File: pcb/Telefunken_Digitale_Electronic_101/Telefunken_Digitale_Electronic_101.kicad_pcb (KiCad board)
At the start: 2 copper layers, 100 x 52 mm, 31 parts, among them J1 Conn_01x02_MountingPin, J2 Conn_01x02_MountingPin, J3 Conn_01x04_MountingPin, J4 Conn_01x02_Socket, J5 Conn_01x02_Socket, J6 Conn_01x02_Socket, J7 Conn_01x02_Socket, J8 Conn_01x02_Socket, SW1 SW_Push, SW2 SW_Push, U1 DS3231, U2 TM1637_SOP20

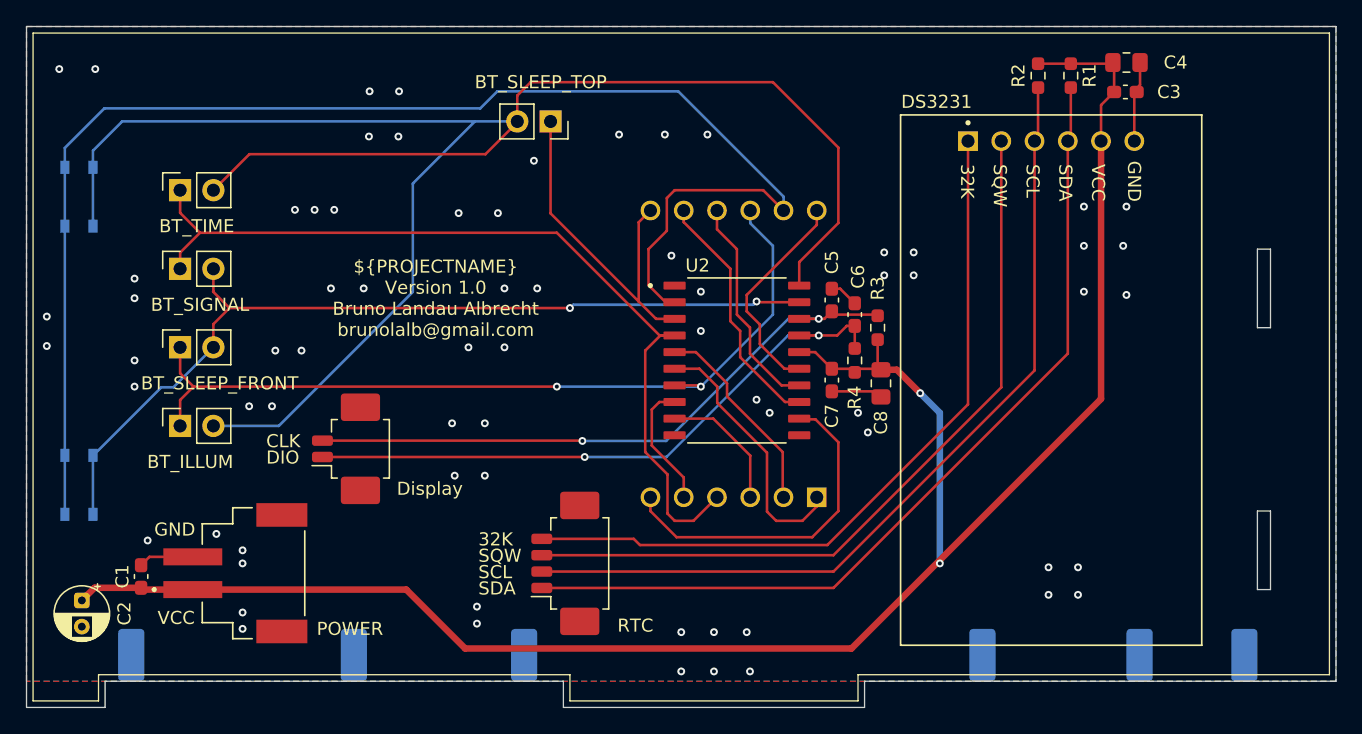
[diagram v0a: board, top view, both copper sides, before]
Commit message: TFK: sch - i2c resistors not populate, logo; pcb - spaced tracks, stitching vias, logo
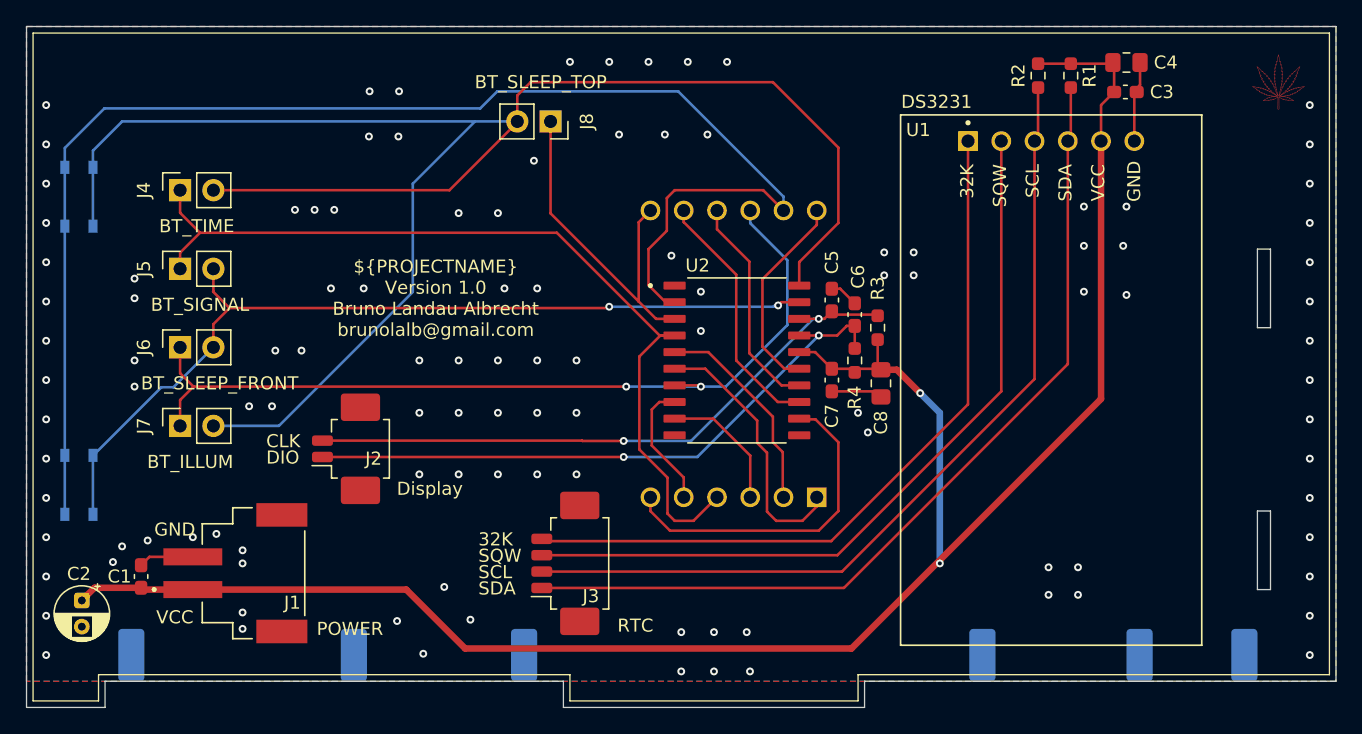
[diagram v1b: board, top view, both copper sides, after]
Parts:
- added LF1: ~, RadioWecker:LEAF, F.Cu at (195.6, 54.3)
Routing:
- net /Buttons/GRID4: track 64.1 -> 66.1 mm
- net Net-(DISPLAY1-CA1): track 16.6 -> 15.6 mm
- net Net-(DISPLAY1-d): track 15.5 -> 16.0 mm
- net GND: vias 70 -> 113

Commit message: TFK: pcb - identification label consistent with core PCB
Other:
- board text added: "${PROJECTNAME} Version ${REVISION} ${ISSUE_DATE} ${COMPANY}"
- board text removed: "${PROJECTNAME} Version ${REVISION} ${COMMENT1} ${COMPANY}"
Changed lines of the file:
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@@
 	(title_block
 		(title "Telefunken_Digitale_Electronic_101 - Display")
-		(date "2026-06-19")
+		(date "2026-07-30")
 		(rev "1.0")
 		(company "brunolalb@gmail.com")
@@
 		)
 	)
-	(gr_text "${PROJECTNAME}\nVersion ${REVISION}\n${COMMENT1}\n${COMPANY}"
+	(gr_text "${PROJECTNAME}\nVersion ${REVISION}\n${ISSUE_DATE}\n${COMPANY}"
 		(at 131.25 73.75 0)
 		(layer "F.SilkS")

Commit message: PCBs: updated logo; added I2C resistors to I2C (core pcb)
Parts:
- removed LF1: ~, RadioWecker:LEAF
- added G1: LOGO, RadioWecker:LOGO, F.Cu at (194.5, 56.0)
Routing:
- net GND: vias 113 -> 112
